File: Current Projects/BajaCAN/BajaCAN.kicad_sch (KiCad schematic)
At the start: 35 parts, among them J1 348300801, U1 AVR128DB32x-xRXB, U2 MCP1603, U3 MCP251863T-H-SS, Y1 OV-7604-C7, Y2 CSTNE20M0V530000R0

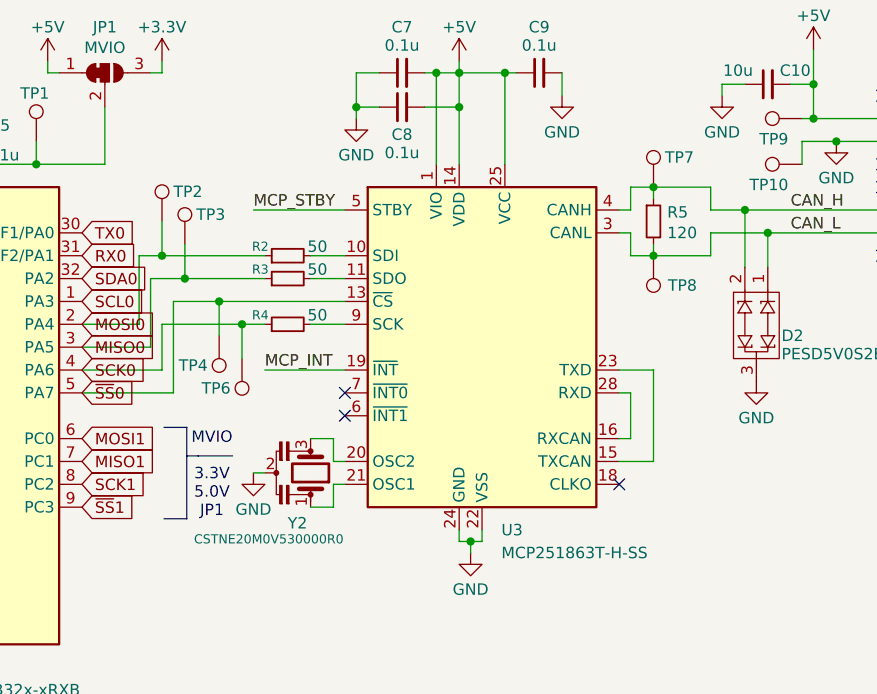
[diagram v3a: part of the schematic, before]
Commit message: Beginning footprint change on Baja CAN
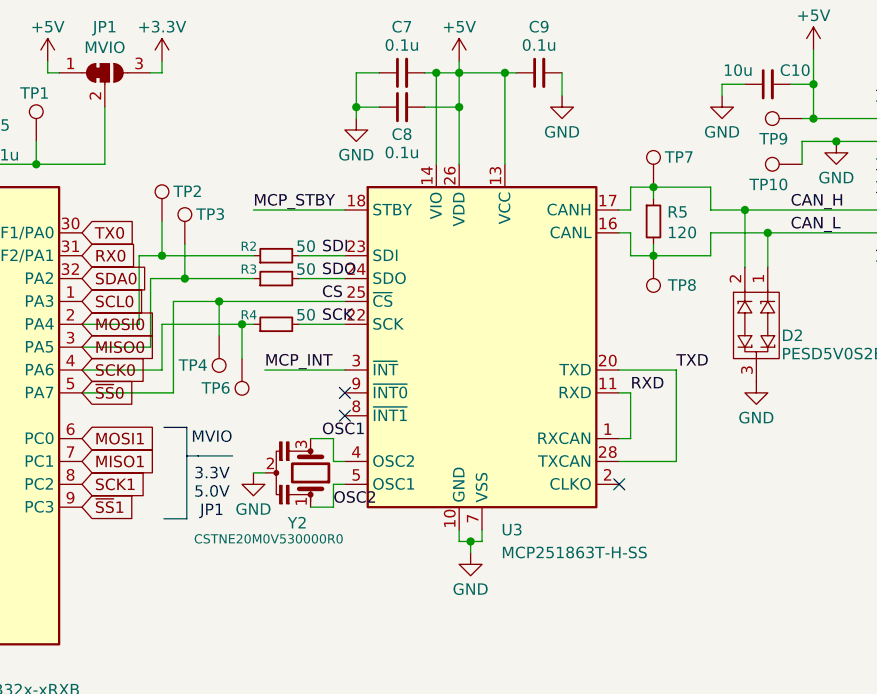
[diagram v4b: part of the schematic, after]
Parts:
- U3: footprint Package_SO:SSOP-28_5.3x10.2mm_P0.65mm -> Package_DFN_QFN:VQFN-28-1EP_5x5mm_P0.5mm_EP3.25x3.25mm; symbol Interface_CAN_LIN:MCP251863T-H-SS -> Interface_CAN_LIN:MCP251863T-E-9PX
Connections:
- net +5V: now also U3.13 (VCC), U3.26 (VDD); no longer U3.1 (VIO), U3.25 (VCC)
- net CAN_H: now also U3.17 (CANH); no longer U3.4 (CANH)
- net CAN_L: now also U3.16 (CANL); no longer U3.3 (CANL)
- net GND: now also U3.10 (GND), U3.7 (VSS); no longer U3.22 (VSS), U3.24 (GND)
- net MCP_INT: now also U3.3 (~{INT}); no longer U3.19 (~{INT})
- net MCP_STBY: now also U3.18 (STBY); no longer U3.5 (STBY)
- net ~{SS}0: now also U3.25 (~{CS}); no longer U3.13 (~{CS})
- net at U3.21 (NC): no longer Y2.1
- net OSC1: now reaches Y2.3
- net OSC1: now also U3.4 (OSC2); no longer U3.20 (OSC2)
- net SDI: now reaches R2.2
- net SDI: now also U3.23 (SDI); no longer U3.10 (SDI)
- net RXD: now reaches U3.11 (RXD)
- net RXD: now also U3.1 (RXCAN); no longer R3.2
- net at U3.15 (NC): no longer U3.23 (TXD)
- net TXD: now reaches U3.28 (TXCAN)
- net TXD: now also U3.20 (TXD); no longer U3.16 (RXCAN)
- net at U3.9 (~{INT0}): no longer R4.2
- new net OSC2: U3.5 (OSC1), Y2.1
- new net SCK: R4.2, U3.22 (SCK)
- new net SDO: R3.2, U3.24 (SDO)
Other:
- moved on the sheet: R2, R3, R4
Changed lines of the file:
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@@
 	(wire
 		(pts
+			(xy 120.65 82.55) (xy 123.19 82.55)
+		)
+		(stroke
+			(width 0)
+			(type default)
+		)
+	)
+	(wire
+		(pts
 			(xy 74.93 41.91) (xy 74.93 52.07)
 		)
@@
 	(wire
 		(pts
-			(xy 120.65 69.85) (xy 124.46 69.85)
+			(xy 119.38 69.85) (xy 124.46 69.85)
 		)
 		(stroke
@@
 	(wire
 		(pts
-			(xy 120.65 62.23) (xy 124.46 62.23)
+			(xy 119.38 62.23) (xy 124.46 62.23)
 		)
 		(stroke
@@
 	(wire
 		(pts
-			(xy 113.03 69.85) (xy 115.57 69.85)
+			(xy 113.03 69.85) (xy 114.3 69.85)
 		)
 		(stroke
@@
 	(wire
 		(pts
-			(xy 120.65 64.77) (xy 124.46 64.77)
+			(xy 119.38 64.77) (xy 124.46 64.77)
 		)
 		(stroke
@@
 	(wire
 		(pts
-			(xy 158.75 74.93) (xy 158.75 85.09)
+			(xy 161.29 74.93) (xy 161.29 85.09)
 		)
 		(stroke
@@
 	(wire
 		(pts
-			(xy 154.94 74.93) (xy 158.75 74.93)
+			(xy 154.94 74.93) (xy 161.29 74.93)
 		)
 		(stroke
@@
 	(wire
 		(pts
-			(xy 158.75 85.09) (xy 154.94 85.09)
+			(xy 161.29 85.09) (xy 154.94 85.09)
 		)
 		(stroke
@@
 	(wire
 		(pts
-			(xy 104.14 62.23) (xy 115.57 62.23)
+			(xy 104.14 62.23) (xy 114.3 62.23)
 		)
 		(stroke
@@
 	(wire
 		(pts
-			(xy 106.68 64.77) (xy 115.57 64.77)
+			(xy 106.68 64.77) (xy 114.3 64.77)
 		)
 		(stroke
@@
 	(wire
 		(pts
-			(xy 120.65 82.55) (xy 123.19 82.55)
-		)
-		(stroke
-			(width 0)
-			(type default)
-		)
-	)
-	(wire
-		(pts
 			(xy 137.16 92.71) (xy 137.16 93.98)
 		)
@@
 		)
 	)
+	(label "SDI"
+		(at 121.92 62.23 0)
+		(effects
+			(font
+				(size 1.27 1.27)
+			)
+			(justify left bottom)
+		)
+	)
+	(label "SDO"
+		(at 121.92 64.77 0)
+		(effects
+			(font
+				(size 1.27 1.27)
+			)
+			(justify left bottom)
+		)
+	)
+	(label "CS"
+		(at 121.92 67.31 0)
+		(effects
+			(font
+				(size 1.27 1.27)
+			)
+			(justify left bottom)
+		)
+	)
+	(label "SCK"
+		(at 121.92 69.85 0)
+		(effects
+			(font
+				(size 1.27 1.27)
+			)
+			(justify left bottom)
+		)
+	)
 	(label "MCP_STBY"
 		(at 44.45 85.09 0)
@@
 		)
 	)
+	(label "RXD"
+		(at 156.21 77.47 0)
+		(effects
+			(font
+				(size 1.27 1.27)
+			)
+			(justify left bottom)
+		)
+	)
+	(label "TXD"
+		(at 161.29 74.93 0)
+		(effects
+			(font
+				(size 1.27 1.27)
+			)
+			(justify left bottom)
+		)
+	)
+	(label "OSC1"
+		(at 121.92 82.55 0)
+		(effects
+			(font
+				(size 1.27 1.27)
+			)
+			(justify left bottom)
+		)
+	)
+	(label "OSC2"
+		(at 123.19 90.17 0)
+		(effects
+			(font
+				(size 1.27 1.27)
+			)
+			(justify left bottom)
+		)
+	)
 	(global_label "PD7"
 		(shape input)
@@
 		(lib_name "R_Small_1")
 		(lib_id "Device:R_Small")
-		(at 118.11 62.23 90)
+		(at 116.84 62.23 90)
 		(unit 1)
 		(exclude_from_sim no)
@@
 		(dnp no)
 		(property "Reference" "R2"
-			(at 115.062 61.214 90)
+			(at 113.792 61.214 90)
 			(effects
 				(font
@@
 		)
 		(property "Value" "50"
-			(at 121.412 61.214 90)
+			(at 120.142 61.214 90)
 			(effects
 				(font
@@
 		)
 		(property "Footprint" "Resistor_SMD:R_0603_1608Metric"
-			(at 118.11 62.23 0)
+			(at 116.84 62.23 0)
 			(effects
 				(font
@@
 		)
 		(property "Datasheet" "~"
-			(at 118.11 62.23 0)
+			(at 116.84 62.23 0)
 			(effects
 				(font
@@
 		)
 		(property "Description" "Resistor, small symbol"
-			(at 118.11 62.23 0)
+			(at 116.84 62.23 0)
 			(effects
 				(font
@@
 		(lib_name "R_Small_1")
 		(lib_id "Device:R_Small")
-		(at 118.11 64.77 90)
+		(at 116.84 64.77 90)
 		(unit 1)
 		(exclude_from_sim no)
@@
 		(dnp no)
 		(property "Reference" "R3"
-			(at 115.062 63.754 90)
+			(at 113.792 63.754 90)
 			(effects
 				(font
@@
 		)
 		(property "Value" "50"
-			(at 121.412 63.754 90)
+			(at 120.142 63.754 90)
 			(effects
 				(font
@@
 		)
 		(property "Footprint" "Resistor_SMD:R_0603_1608Metric"
-			(at 118.11 64.77 0)
+			(at 116.84 64.77 0)
 			(effects
 				(font
@@
 		)
 		(property "Datasheet" "~"
-			(at 118.11 64.77 0)
+			(at 116.84 64.77 0)
 			(effects
 				(font
@@
 		)
 		(property "Description" "Resistor, small symbol"
-			(at 118.11 64.77 0)
+			(at 116.84 64.77 0)
 			(effects
 				(font
@@
 	)
 	(symbol
-		(lib_id "Interface_CAN_LIN:MCP251863T-H-SS")
+		(lib_id "Interface_CAN_LIN:MCP251863T-E-9PX")
 		(at 139.7 72.39 0)
 		(unit 1)
@@
 			)
 		)
-		(property "Footprint" "Package_SO:SSOP-28_5.3x10.2mm_P0.65mm"
+		(property "Footprint" "Package_DFN_QFN:VQFN-28-1EP_5x5mm_P0.5mm_EP3.25x3.25mm"
 			(at 144.78 99.06 0)
 			(effects
@@
 			)
 		)
-		(property "Description" "External CAN FD Controller with Integrated Transceiver, SSOP-28"
+		(property "Description" "External CAN FD Controller with Integrated Transceiver, VQFN-28"
 			(at 171.958 94.234 0)
 			(effects
@@
 		(pin "25"
 		)
-		(pin "27"
+		(pin "29"
 		)
 		(pin "17"
@@
 		(lib_name "R_Small_1")
 		(lib_id "Device:R_Small")
-		(at 118.11 69.85 90)
+		(at 116.84 69.85 90)
 		(unit 1)
 		(exclude_from_sim no)
@@
 		(dnp no)
 		(property "Reference" "R4"
-			(at 115.062 68.834 90)
+			(at 113.792 68.834 90)
 			(effects
 				(font
@@
 		)
 		(property "Value" "50"
-			(at 121.412 68.834 90)
+			(at 120.142 68.834 90)
 			(effects
 				(font
@@
 		)
 		(property "Footprint" "Resistor_SMD:R_0603_1608Metric"
-			(at 118.11 69.85 0)
+			(at 116.84 69.85 0)
 			(effects
 				(font
@@
 		)
 		(property "Datasheet" "~"
-			(at 118.11 69.85 0)
+			(at 116.84 69.85 0)
 			(effects
 				(font
@@
 		)
 		(property "Description" "Resistor, small symbol"
-			(at 118.11 69.85 0)
+			(at 116.84 69.85 0)
 			(effects
 				(font

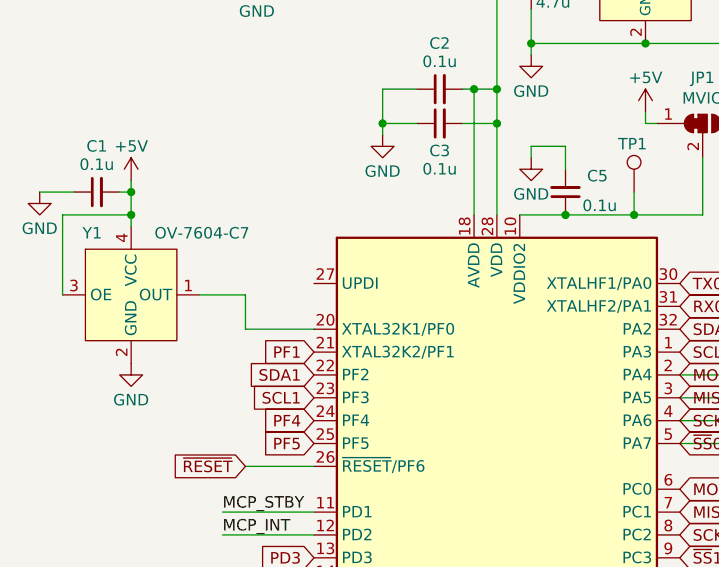
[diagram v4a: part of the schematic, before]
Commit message: Fixed final BajaCAN DRC errors
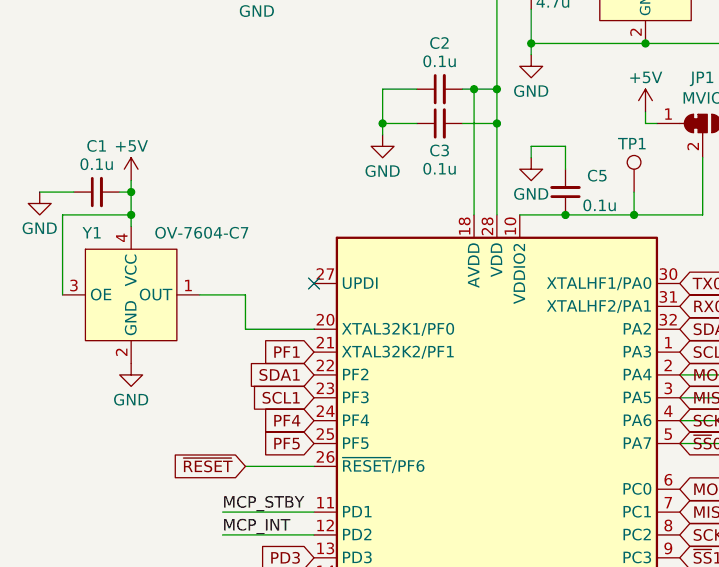
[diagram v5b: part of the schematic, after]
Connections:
- no-connect marks 7 -> 8
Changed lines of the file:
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@@
+	)
+	(no_connect
+		(at 54.61 59.69)
 	)
 	(no_connect

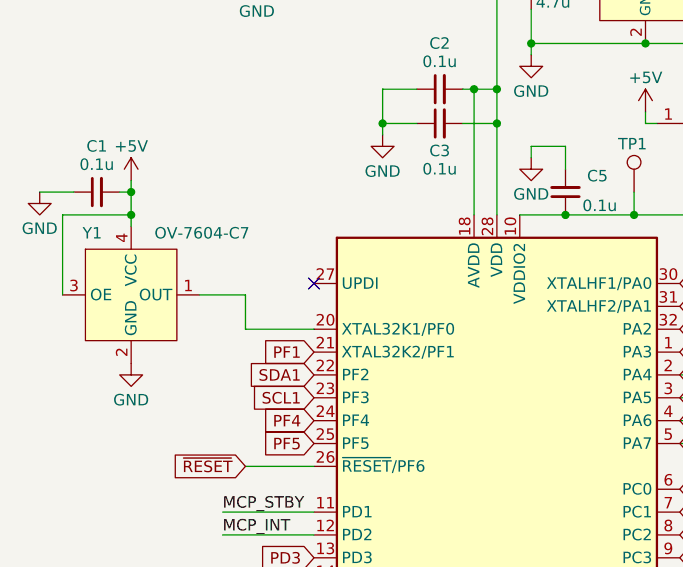
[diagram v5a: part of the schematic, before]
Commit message: CANNode: reworked Prog header; slightly improved routing; DRC verified
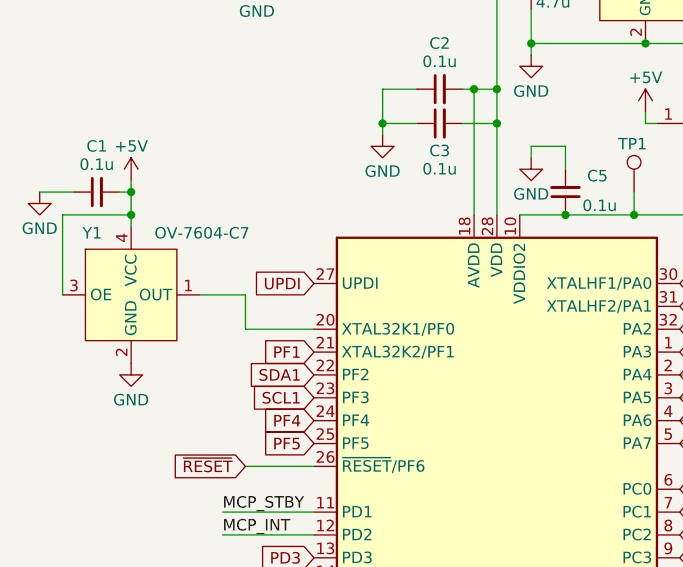
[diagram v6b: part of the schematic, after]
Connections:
- net UPDI: now reaches U1.27 (UPDI)
- no-connect marks 8 -> 7
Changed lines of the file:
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@@
-	)
-	(no_connect
-		(at 54.61 59.69)
 	)
 	(no_connect
@@
 			(effects
 				(font
+					(size 1.27 1.27)
+				)
+				(justify right)
+				(hide yes)
+			)
+		)
+	)
+	(global_label "UPDI"
+		(shape input)
+		(at 54.61 59.69 180)
+		(fields_autoplaced yes)
+		(effects
+			(font
+				(size 1.27 1.27)
+			)
+			(justify right)
+		)
+		(property "Intersheetrefs" "${INTERSHEET_REFS}"
+			(at 47.1495 59.69 0)
+			(effects
+				(font

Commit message: Schematic Annotations (no board changes)
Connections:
- net OSC1: no longer names the net of U3.4 (OSC2), Y2.3
- net OSC2: no longer names the net of U3.5 (OSC1), Y2.1
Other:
- note added: "3.3V SUPPLY"
- note added: "32.768kHz MILLISECOND TIMING REFERENCE"
- note added: "@ 500 mA MAX"
- note added: "CAN CLOCK 20 MHz"
- note added: "CAN I/O Bus Power In"
- note added: "Integrated CAN Controller/Transceiver"
- note added: "MCU"
- note added: "MVIO SELECT"
- note added: "Note: TXD to TXCAN, RXD to RXCAN. Counterintuitive, but per datasheet"
- note added: "ONLY POPULATE R5 AT BUS END NODES"
- note added: "POWER LED"
- note added: "R2, R3, R4 reduce ringing on SPI lines. Place near receiving line end."
- note added: "TIMING XTAL"
- moved on the sheet: C10, C7, C8, C9, D1, D2, J1, R1, R2, R3, R4, R5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

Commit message: Sheet references
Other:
- company: NCSU Baja -> Pack Motorsports Baja
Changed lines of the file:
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@@
 	(title_block
 		(title "NCSU Baja CAN Node")
-		(date "2025-09-06")
-		(rev "1")
-		(company "NCSU Baja")
+		(date "2025-11-10")
+		(rev "2")
+		(company "Pack Motorsports Baja")
+		(comment 1 "Engineer: Jacob Hahn")
+		(comment 2 "Designed in Raleigh, NC")
 	)
 	(circle
